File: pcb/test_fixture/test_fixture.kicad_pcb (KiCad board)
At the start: 2 copper layers, 71.5 x 74.9 mm, 79 parts, among them J1 UART, J3 Conn_ARM_JTAG_SWD_10, J5 GND, J6 GND, P3.3V1 , U1 SC0915, U2 MIC29302WU, U3 INA186A5IDCKR, U4 INA186A5IDCKR

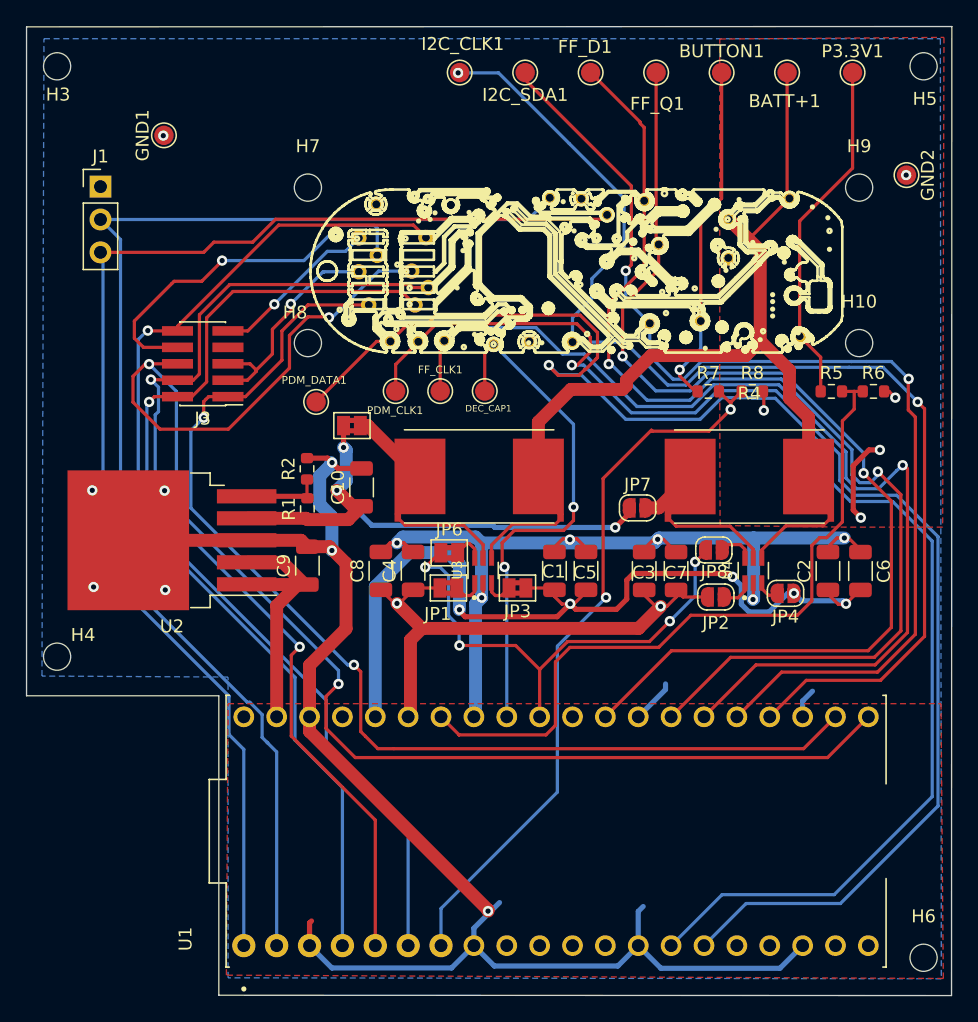
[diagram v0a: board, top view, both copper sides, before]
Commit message: [pcb] fixed few issues with fixture, filled in all LCSC IDs for the fixture
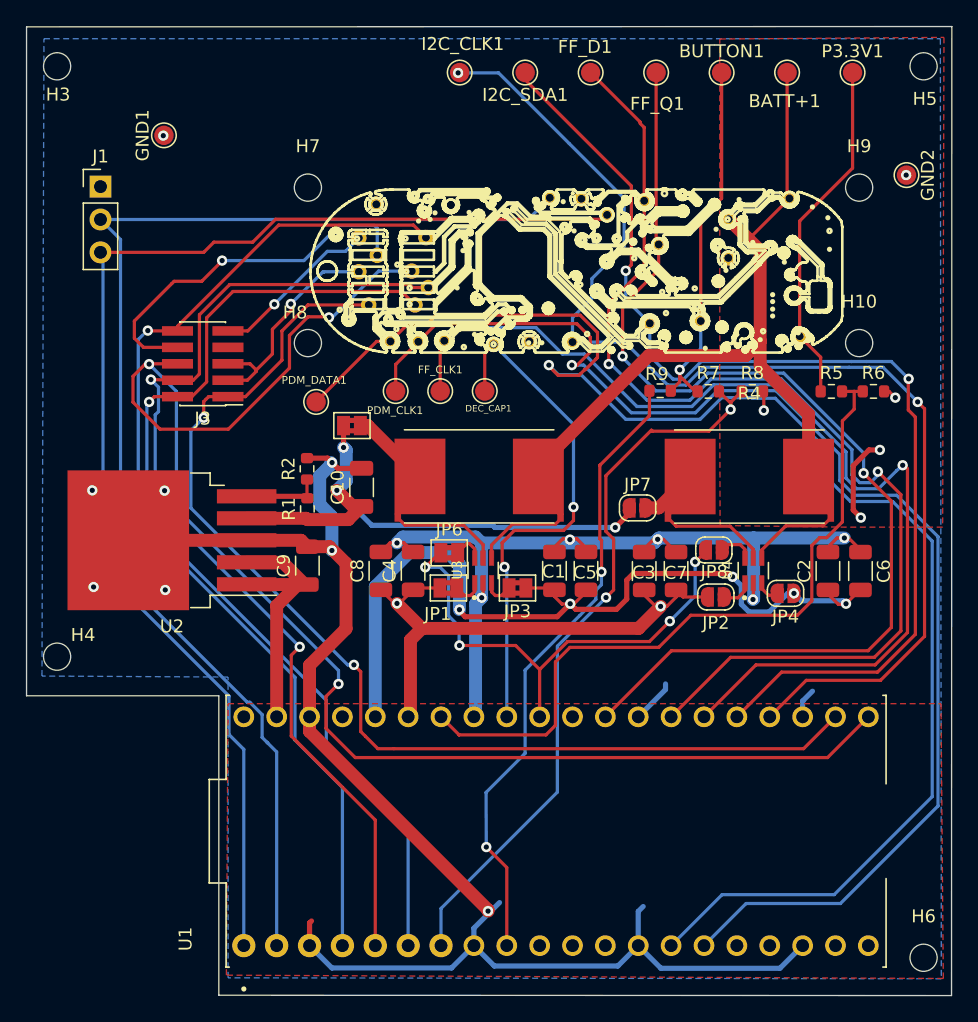
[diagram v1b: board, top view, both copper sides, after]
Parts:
- added R9: 1K, Resistor_SMD:R_0603_1608Metric, F.Cu at (130.7, 96.5)
- C10: footprint Resistor_SMD:R_1206_3216Metric -> Capacitor_SMD:C_1206_3216Metric
- R5, R6: value 1M -> 100K
- R7: value 2M -> 200K
- R8: value 3M -> 300K
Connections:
- net /POWER_VBAT renamed /BATT+
- U1 pad 9: unconnected-(U1-Pad9) -> Net-(U1-Pad9)
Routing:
- net Net-(U1-Pad9): track 0.00 -> 48.9 mm, vias 0 -> 2
- net /BATT+: track 75.2 -> 72.9 mm
- net /BUTTON: track 26.9 -> 28.3 mm
